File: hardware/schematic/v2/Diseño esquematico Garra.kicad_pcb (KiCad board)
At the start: 2 copper layers, 15 parts

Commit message: PCB progress
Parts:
- added C2: C_100uF, Capacitor_THT:C_Radial_D8.0mm_H11.5mm_P3.50mm, F.Cu at (37.2, 46.0)
- moved C1 87.1 mm to (27.2, 46.0)
- moved Pin_Buttons_2 75.6 mm to (44.0, 100.5)
- moved Pin_EDU-CIAA_to_ESP1 73.4 mm to (156.5, 27.9)
- moved V1 70.1 mm to (30.2, 29.4), turned to -90 degrees
- moved DRV8825_1 69.0 mm to (140.7, 59.2)
- moved Bornier_Nema17_2 67.3 mm to (139.8, 102.9)
- moved Pin_Buttons_1 52.7 mm to (59.5, 101.5)
- moved Bornier_Nema17_1 48.6 mm to (116.3, 103.0)
- moved Bornier_DRV8833 41.2 mm to (95.4, 103.0)
- moved DRV8833 40.6 mm to (32.7, 68.1)
- moved Bornier_Servo1 37.4 mm to (72.8, 103.0)
- moved DRV8825_2 33.5 mm to (117.3, 59.3)
- moved XL4005 19.5 mm to (91.7, 28.1)
- moved CIAA-P1 9.57 mm to (99.2, 67.5)
- moved CIAA-P2 9.57 mm to (102.5, 67.5)

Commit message: PCB progress
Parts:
- moved C1 103.8 mm to (131.0, 42.8)
- moved C2 103.8 mm to (141.0, 42.8)
- moved DRV8833 59.7 mm to (91.7, 59.1)
- moved XL4005 44.4 mm to (47.3, 26.2)
- moved CIAA-P2 30.8 mm to (71.7, 68.1), turned to -90 degrees
- moved CIAA-P1 27.6 mm to (71.7, 64.8), turned to -90 degrees

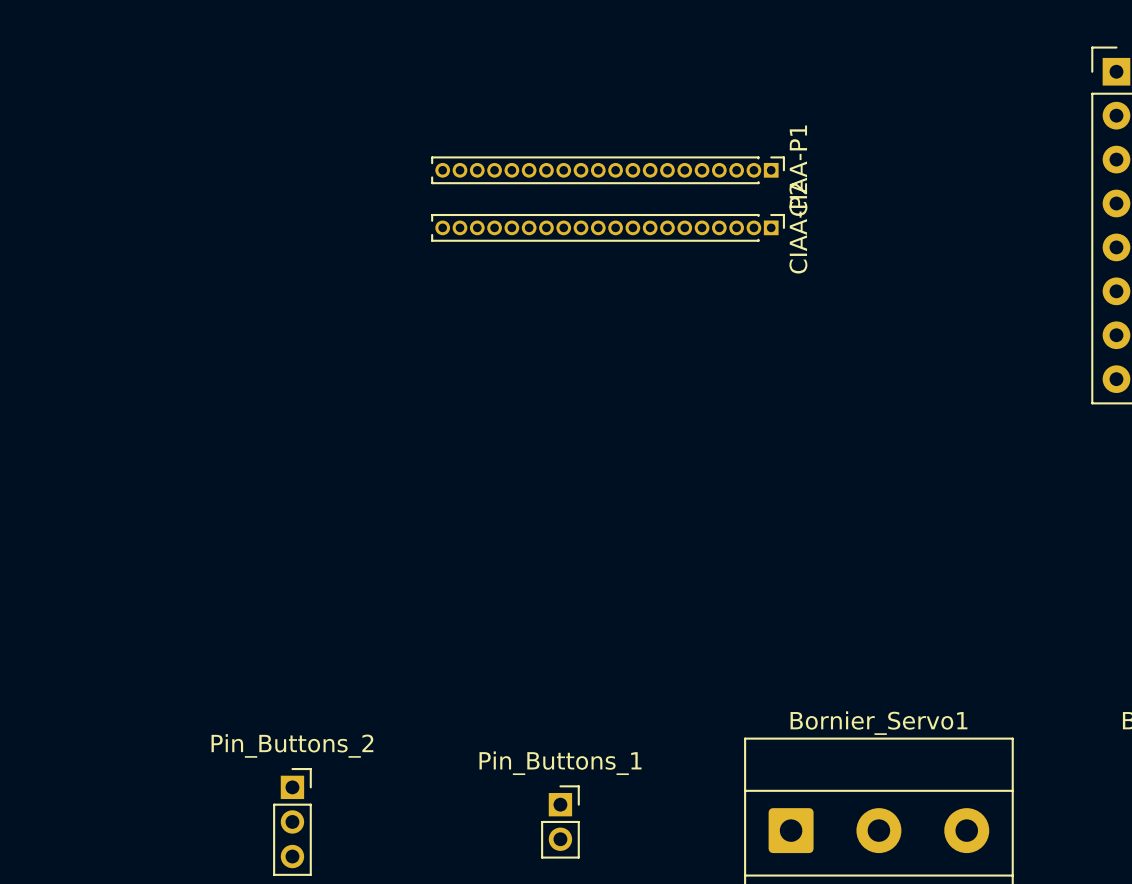
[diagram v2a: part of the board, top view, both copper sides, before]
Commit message: Official EDU-CIAA footprints added
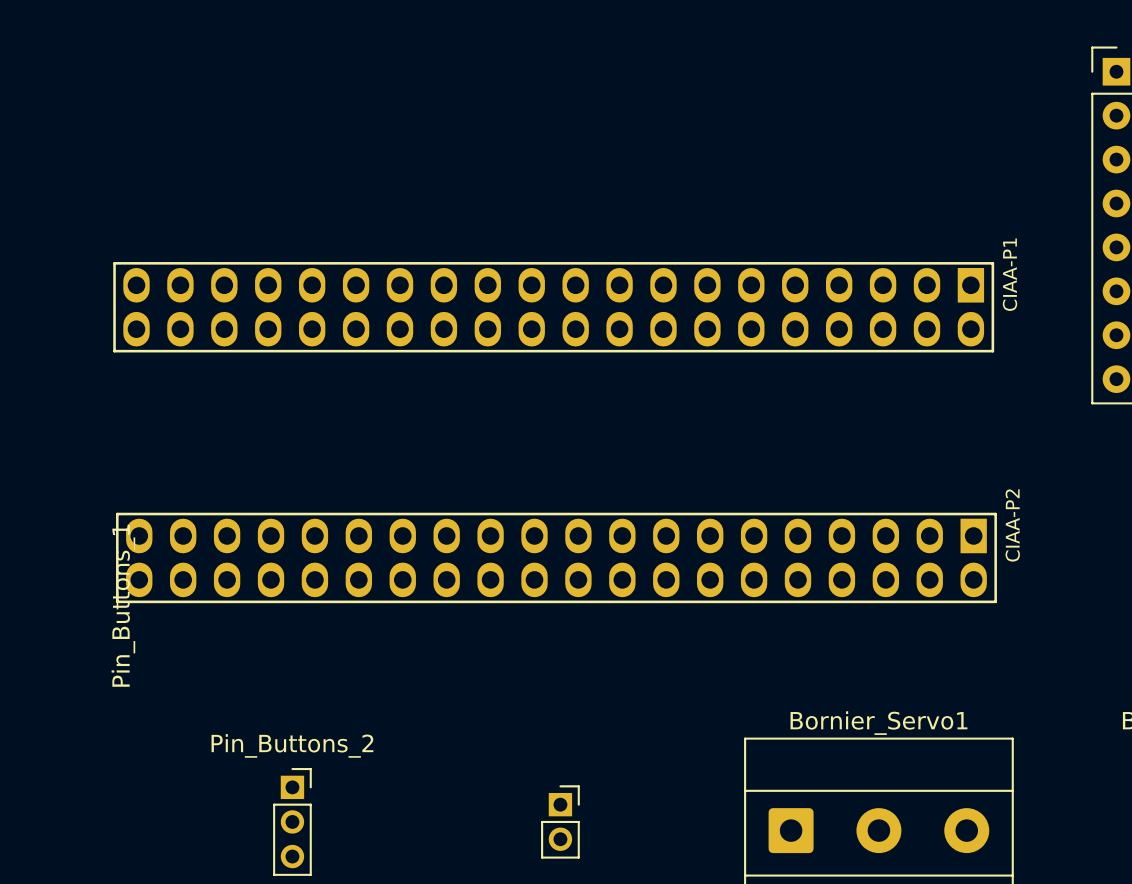
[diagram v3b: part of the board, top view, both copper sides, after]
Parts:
- CIAA-P1, CIAA-P2: footprint Connector_PinHeader_1.00mm:PinHeader_1x20_P1.00mm_Vertical -> Libreria_EDU_CIAA_NXP:PIN_ARRAY_20X2
- moved CIAA-P2 22.8 mm to (59.3, 87.2), turned to 180 degrees
- moved CIAA-P1 14.9 mm to (59.1, 72.7), turned to 180 degrees

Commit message: PCB Updated
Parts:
- removed Pin_Buttons_2: Pin_Terminal_01x06, Connector_PinSocket_2.00mm:PinSocket_1x03_P2.00mm_Vertical
- added PinOut_B_DWN: Pin_Terminal_01x05, Connector_PinSocket_2.00mm:PinSocket_1x02_P2.00mm_Vertical, F.Cu at (30.5, 107.0)
- added PinOut_B_UP: Pin_Terminal_01x05, Connector_PinSocket_2.00mm:PinSocket_1x02_P2.00mm_Vertical, F.Cu at (42.0, 107.0)
- added PinOut_POT: Pin_Terminal_01x05, Connector_PinSocket_2.00mm:PinSocket_1x02_P2.00mm_Vertical, F.Cu at (30.5, 100.0)
- PinOut_Stick: renamed from Pin_Buttons_1; footprint Connector_PinSocket_2.00mm:PinSocket_1x02_P2.00mm_Vertical -> Connector_PinSocket_2.00mm:PinSocket_1x04_P2.00mm_Vertical
- moved CIAA-P2 12.5 mm to (54.3, 75.8)
- moved CIAA-P1 12.5 mm to (54.1, 61.3)
- moved PinOut_Stick 8.00 mm to (51.5, 101.5)
- moved C2 3.26 mm to (144.2, 43.0)
- moved PinOut_UART1 2.93 mm to (154.0, 29.5)
- renumbered Bornier_DRV8833 to Bornier_DRV833, DRV8833 to DRV833, Pin_EDU-CIAA_to_ESP1 to PinOut_UART1, V1 to V_Input
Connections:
- C1 pad 1: VMOT -> 12V
- C1 pad 2: GND_A -> GND
- C2 pad 1: (no net) -> 12V
- C2 pad 2: (no net) -> GND
- CIAA-P1 pad 20: GND_B2 -> GND_B_UP
- CIAA-P1 pad 22: GND_B1 -> GND_B_DWN
- DRV8825_1 pad 7: GND_A_C1 -> GND
- DRV8825_1 pad 8: VMOT_C1 -> 12V
- DRV8825_2 pad 7: GND_A_C2 -> GND
- DRV8825_2 pad 8: VMOT_C2 -> 12V
- V_Input pad 1: VMOT -> 12V
- V_Input pad 2: GND_A -> GND
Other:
- board text added: "GND"
- board text added: "SW"
- board text added: "VRX"
- board text added: "VRY"

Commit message: PCB updated
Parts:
- moved DRV833 80.7 mm to (166.2, 28.3)
- moved DRV8825_1 80.7 mm to (215.3, 28.4)
- moved DRV8825_2 80.7 mm to (191.9, 28.4)
- moved XL4005 66.3 mm to (108.8, 50.8)
- moved CIAA-P2 48.5 mm to (73.8, 31.4)
- moved CIAA-P1 46.1 mm to (73.8, 103.0)
- moved Bornier_DRV833 27.3 mm to (98.0, 130.2)
- moved Bornier_Nema17_1 27.3 mm to (118.8, 130.2)
- moved Bornier_Servo1 27.3 mm to (75.4, 130.2)
- moved PinOut_B_DWN 27.3 mm to (33.1, 134.2)
- moved PinOut_B_UP 27.3 mm to (44.6, 134.2)
- moved PinOut_Stick 27.3 mm to (54.1, 128.7)
- moved Bornier_Nema17_2 27.3 mm to (142.4, 130.1)
- moved PinOut_POT 27.3 mm to (33.1, 127.2)
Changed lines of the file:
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@@
 	(footprint "Connector_PinSocket_2.00mm:PinSocket_1x04_P2.00mm_Vertical"
 		(layer "F.Cu")
-		(at 51.5 101.5)
+		(at 54.075 128.6725)
 		(descr "Through hole straight socket strip, 1x04, 2.00mm pitch, single row (from Kicad 4.0.7), script generated")
 		(tags "Through hole socket strip THT 1x04 2.00mm single row")
@@
 	(footprint "Module:Pololu_Breakout-16_15.2x20.3mm"
 		(layer "F.Cu")
-		(at 91.66 59.11)
+		(at 166.232503 28.294837)
 		(descr "Pololu Breakout 16-pin 15.2x20.3mm 0.6x0.8")
 		(tags "Pololu Breakout")
@@
 	(footprint "Connector_PinSocket_2.00mm:PinSocket_1x02_P2.00mm_Vertical"
 		(layer "F.Cu")
-		(at 42 107 -90)
+		(at 44.575 134.1725 -90)
 		(descr "Through hole straight socket strip, 1x02, 2.00mm pitch, single row (from Kicad 4.0.7), script generated")
 		(tags "Through hole socket strip THT 1x02 2.00mm single row")
@@
 	(footprint "Module:Pololu_Breakout-16_15.2x20.3mm"
 		(layer "F.Cu")
-		(at 140.727497 59.195163)
+		(at 215.3 28.38)
 		(descr "Pololu Breakout 16-pin 15.2x20.3mm 0.6x0.8")
 		(tags "Pololu Breakout")
@@
 	(footprint "TerminalBlock_Phoenix:TerminalBlock_Phoenix_MKDS-1,5-4-5.08_1x04_P5.08mm_Horizontal"
 		(layer "F.Cu")
-		(at 116.26 103)
+		(at 118.835 130.1725)
 		(descr "Terminal Block Phoenix MKDS-1,5-4-5.08, 4 pins, pitch 5.08mm, size 20.3x9.8mm, drill diameter 1.3mm, pad diameter 2.6mm, http://www.farnell.com/datasheets/100425.pdf, script-generated using https://gitlab.com/kicad/libraries/kicad-footprint-generator/-/tree/master/scripts/TerminalBlock_Phoenix")
 		(tags "THT Terminal Block Phoenix MKDS-1,5-4-5.08 pitch 5.08mm size 20.3x9.8mm drill 1.3mm pad 2.6mm")
@@
 	(footprint "TerminalBlock_Phoenix:TerminalBlock_Phoenix_MKDS-1,5-3-5.08_1x03_P5.08mm_Horizontal"
 		(layer "F.Cu")
-		(at 72.84 103)
+		(at 75.415 130.1725)
 		(descr "Terminal Block Phoenix MKDS-1,5-3-5.08, 3 pins, pitch 5.08mm, size 15.2x9.8mm, drill diameter 1.3mm, pad diameter 2.6mm, http://www.farnell.com/datasheets/100425.pdf, script-generated using https://gitlab.com/kicad/libraries/kicad-footprint-generator/-/tree/master/scripts/TerminalBlock_Phoenix")
 		(tags "THT Terminal Block Phoenix MKDS-1,5-3-5.08 pitch 5.08mm size 15.2x9.8mm drill 1.3mm pad 2.6mm")
@@
 	(footprint "Libreria_EDU_CIAA_NXP:PIN_ARRAY_20X2"
 		(layer "F.Cu")
-		(at 54.27 75.77 180)
+		(at 73.8 31.4 180)
 		(descr "Double rangee de contacts 2 x 12 pins")
 		(tags "CONN")
 		(property "Reference" "CIAA-P2"
-			(at -26.42 1.9 90)
+			(at -26.7 -0.1 90)
 			(layer "F.SilkS")
 			(effects
@@
 	(footprint "Connector_PinSocket_2.00mm:PinSocket_1x02_P2.00mm_Vertical"
 		(layer "F.Cu")
-		(at 30.5 107 -90)
+		(at 33.075 134.1725 -90)
 		(descr "Through hole straight socket strip, 1x02, 2.00mm pitch, single row (from Kicad 4.0.7), script generated")
 		(tags "Through hole socket strip THT 1x02 2.00mm single row")
@@
 	(footprint "Libreria_EDU_CIAA_NXP:PIN_ARRAY_20X2"
 		(layer "F.Cu")
-		(at 54.11 61.27 180)
+		(at 73.8 103 180)
 		(descr "Double rangee de contacts 2 x 12 pins")
 		(tags "CONN")
 		(property "Reference" "CIAA-P1"
-			(at -26.42 1.9 90)
+			(at -26.7 0 90)
 			(layer "F.SilkS")
 			(effects
@@
 	(footprint "TerminalBlock_Phoenix:TerminalBlock_Phoenix_MKDS-1,5-2-5.08_1x02_P5.08mm_Horizontal"
 		(layer "F.Cu")
-		(at 95.42 103)
+		(at 97.995 130.1725)
 		(descr "Terminal Block Phoenix MKDS-1,5-2-5.08, 2 pins, pitch 5.08mm, size 10.2x9.8mm, drill diameter 1.3mm, pad diameter 2.6mm, http://www.farnell.com/datasheets/100425.pdf, script-generated using https://gitlab.com/kicad/libraries/kicad-footprint-generator/-/tree/master/scripts/TerminalBlock_Phoenix")
 		(tags "THT Terminal Block Phoenix MKDS-1,5-2-5.08 pitch 5.08mm size 10.2x9.8mm drill 1.3mm pad 2.6mm")
@@
 	(footprint "Module:Pololu_Breakout-16_15.2x20.3mm"
 		(layer "F.Cu")
-		(at 117.3 59.26)
+		(at 191.872503 28.444837)
 		(descr "Pololu Breakout 16-pin 15.2x20.3mm 0.6x0.8")
 		(tags "Pololu Breakout")
@@
 	(footprint "Module:Pololu_Breakout-16_15.2x20.3mm"
 		(layer "F.Cu")
-		(at 47.258524 26.241022)
+		(at 108.8 50.825)
 		(descr "Pololu Breakout 16-pin 15.2x20.3mm 0.6x0.8")
 		(tags "Pololu Breakout")
@@
 	(footprint "Connector_PinSocket_2.00mm:PinSocket_1x02_P2.00mm_Vertical"
 		(layer "F.Cu")
-		(at 30.5 100 -90)
+		(at 33.075 127.1725 -90)
 		(descr "Through hole straight socket strip, 1x02, 2.00mm pitch, single row (from Kicad 4.0.7), script generated")
 		(tags "Through hole socket strip THT 1x02 2.00mm single row")
@@
 	(footprint "TerminalBlock_Phoenix:TerminalBlock_Phoenix_MKDS-1,5-4-5.08_1x04_P5.08mm_Horizontal"
 		(layer "F.Cu")
-		(at 139.822331 102.911233)
+		(at 142.397331 130.083733)
 		(descr "Terminal Block Phoenix MKDS-1,5-4-5.08, 4 pins, pitch 5.08mm, size 20.3x9.8mm, drill diameter 1.3mm, pad diameter 2.6mm, http://www.farnell.com/datasheets/100425.pdf, script-generated using https://gitlab.com/kicad/libraries/kicad-footprint-generator/-/tree/master/scripts/TerminalBlock_Phoenix")
 		(tags "THT Terminal Block Phoenix MKDS-1,5-4-5.08 pitch 5.08mm size 20.3x9.8mm drill 1.3mm pad 2.6mm")
@@
 	)
 	(gr_text "VRY\n\n"
-		(at 54 105.5 0)
+		(at 56.575 132.6725 0)
 		(layer "F.Cu")
 		(effects
@@
 	)
 	(gr_text "GND"
-		(at 54 106 0)
+		(at 56.575 133.1725 0)
 		(layer "F.Cu")
 		(effects
@@
 	)
 	(gr_text "SW"
-		(at 54 108.5 0)
+		(at 56.575 135.6725 0)
 		(layer "F.Cu")
 		(effects
@@
 	)
 	(gr_text "VRX\n"
-		(at 54 101.5 0)
+		(at 56.575 128.6725 0)
 		(layer "F.Cu")
 		(effects

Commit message: PCB Updated
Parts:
- moved DRV8825_1 166.4 mm to (74.7, 117.3), turned to -90 degrees
- moved DRV8825_2 129.2 mm to (98.2, 117.3), turned to -90 degrees
- moved C1 109.1 mm to (77.8, 138.0), turned to 180 degrees
- moved PinOut_B_DWN1 106.5 mm to (114.5, 65.5)
- moved C2 104.3 mm to (101.2, 138.0), turned to 180 degrees
- moved PinOut_B_UP1 102.7 mm to (114.5, 59.0)
- moved PinOut_POT1 98.4 mm to (114.5, 72.0)
- moved DRV833 92.9 mm to (111.9, 103.7)
- moved CIAA-P2 85.9 mm to (41.9, 111.2), turned to -90 degrees
- moved Bornier_Servo1 83.0 mm to (44.0, 53.3), turned to -90 degrees
- moved V_Input1 81.9 mm to (111.0, 43.0), turned to 90 degrees
- moved Bornier_N20_DC1 79.0 mm to (44.0, 72.5), turned to -90 degrees
- moved PinOut_Stick1 76.1 mm to (96.5, 65.5)
- moved Bornier_Nema17_2 65.2 mm to (81.9, 154.4)
- moved Bornier_Nema17_1 65.2 mm to (58.3, 154.5)
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- renumbered Bornier_DRV833 to Bornier_N20_DC1, PinOut_B_DWN to PinOut_B_DWN1, PinOut_B_UP to PinOut_B_UP1, PinOut_POT to PinOut_POT1, PinOut_Stick to PinOut_Stick1, V_Input to V_Input1
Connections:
- Bornier_Nema17_1 pad 1: B2_1 -> A2_1
- Bornier_Nema17_1 pad 2: B1_1 -> A1_1
- Bornier_Nema17_1 pad 3: A1_1 -> B1_1
- Bornier_Nema17_1 pad 4: A2_1 -> B2_1
- Bornier_Nema17_2 pad 1: B2_2 -> A2_2
- Bornier_Nema17_2 pad 2: B1_2 -> A1_2
- Bornier_Nema17_2 pad 3: A1_2 -> B1_2
- Bornier_Nema17_2 pad 4: A2_2 -> B2_2
- DRV833 pad 10: unconnected-(DRV1-OUT3-Pad10) -> GND
- DRV833 pad 2: unconnected-(DRV1-IN3-Pad2) -> MOTOR_VCC
- DRV833 pad 3: GND -> MOTOR_GND
- DRV833 pad 4: 5V -> unconnected-(DRV833-OUT3-Pad4)
- DRV833 pad 5: IN2 -> unconnected-(DRV833-OUT4-Pad5)
- DRV833 pad 6: IN1 -> unconnected-(DRV833-ULT-Pad6)
- DRV833 pad 7: unconnected-(DRV1-EEP-Pad7) -> IN1
- DRV833 pad 8: MOTOR_VCC -> IN2
- DRV833 pad 9: MOTOR_GND -> 5V
- DRV8825_1 pad 1: GND -> EN1
- DRV8825_1 pad 10: M01 -> unconnected-(DRV8825_1-~{FLT}-Pad10)
- DRV8825_1 pad 11: M11 -> A2_1
- DRV8825_1 pad 12: M21 -> A1_1
- DRV8825_1 pad 13: 5V -> B1_1
- DRV8825_1 pad 14: 5V -> B2_1
- DRV8825_1 pad 15: STEP1 -> GND
- DRV8825_1 pad 16: DIR1 -> 12V
- DRV8825_1 pad 2: unconnected-(DRV8825_1-~{FLT}-Pad2) -> M01
- DRV8825_1 pad 3: A2_1 -> M11
- DRV8825_1 pad 4: A1_1 -> M21
- DRV8825_1 pad 5: B1_1 -> 5V
- DRV8825_1 pad 6: B2_1 -> 5V
- DRV8825_1 pad 7: GND -> STEP1
- DRV8825_1 pad 8: 12V -> DIR1
- DRV8825_1 pad 9: EN1 -> GND
- DRV8825_2 pad 1: GND -> EN2
- DRV8825_2 pad 10: M02 -> unconnected-(DRV8825_2-~{FLT}-Pad10)
- DRV8825_2 pad 11: M12 -> A2_2
- DRV8825_2 pad 12: M22 -> A1_2
- DRV8825_2 pad 13: 5V -> B1_2
- DRV8825_2 pad 14: 5V -> B2_2
- DRV8825_2 pad 15: STEP2 -> GND
- DRV8825_2 pad 16: DIR2 -> 12V
- DRV8825_2 pad 2: unconnected-(DRV8825_2-~{FLT}-Pad2) -> M02
- DRV8825_2 pad 3: A2_2 -> M12
- DRV8825_2 pad 4: A1_2 -> M22
- DRV8825_2 pad 5: B1_2 -> 5V
- DRV8825_2 pad 6: B2_2 -> 5V
- DRV8825_2 pad 7: GND -> STEP2
- DRV8825_2 pad 8: 12V -> DIR2
- DRV8825_2 pad 9: EN2 -> GND

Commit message: feat: PCB routing first stage completed
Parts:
- moved PinOut_Stick1 80.5 mm to (114.5, 144.0)
- moved Bornier_Servo1 67.6 mm to (111.5, 50.5), turned to 90 degrees
- moved V_Input1 67.3 mm to (43.7, 41.4), turned to -90 degrees
- moved Bornier_N20_DC1 63.8 mm to (93.5, 32.3), turned to 180 degrees
- moved C1 34.3 mm to (73.2, 104.0)
- moved C2 34.0 mm to (100.8, 104.0)
- moved XL4005 32.1 mm to (56.8, 53.3), turned to 0 degrees
- moved DRV8825_1 18.3 mm to (57.2, 112.2), turned to 0 degrees
- moved DRV8825_2 14.5 mm to (84.7, 112.1), turned to 0 degrees
- moved DRV833 4.50 mm to (111.9, 99.2)
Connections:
- net TFIL2 renamed SERVO_PWM
- CIAA-P1 pad 33: IN1 -> IN2
- CIAA-P1 pad 35: IN2 -> IN1
- CIAA-P2 pad 36: unconnected-(CIAA-P2-GPIO5-Pad36) -> B_DWN
- CIAA-P2 pad 38: unconnected-(CIAA-P2-GPIO7-Pad38) -> B_UP
- CIAA-P2 pad 40: unconnected-(CIAA-P2-GPIO8-Pad40) -> SW
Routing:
- net B_UP: track 0.00 -> 144.4 mm
- net B_DWN: track 0.00 -> 134.6 mm
- net 12V: track 0.00 -> 132.0 mm
- net SERVO_PWM: track 0.00 -> 93.9 mm
- net SW: track 0.00 -> 84.2 mm
- net MOTOR_GND: track 0.00 -> 61.2 mm
- net EN2: track 0.00 -> 60.5 mm
- net MOTOR_VCC: track 0.00 -> 59.4 mm
- net 5V: track 0.00 -> 58.7 mm
- net VRX: track 0.00 -> 51.2 mm
- net GND_Stick: track 0.00 -> 51.0 mm
- net VRY: track 0.00 -> 50.8 mm
- net RS232_TX: track 0.00 -> 48.3 mm
- net EN1: track 0.00 -> 47.5 mm
- net STEP2: track 0.00 -> 46.8 mm
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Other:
- board outline added: 85.5 x 137 mm
